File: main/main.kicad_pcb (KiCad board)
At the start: 2 copper layers, 1 part, among them M1 IDP_PROTOBOARD

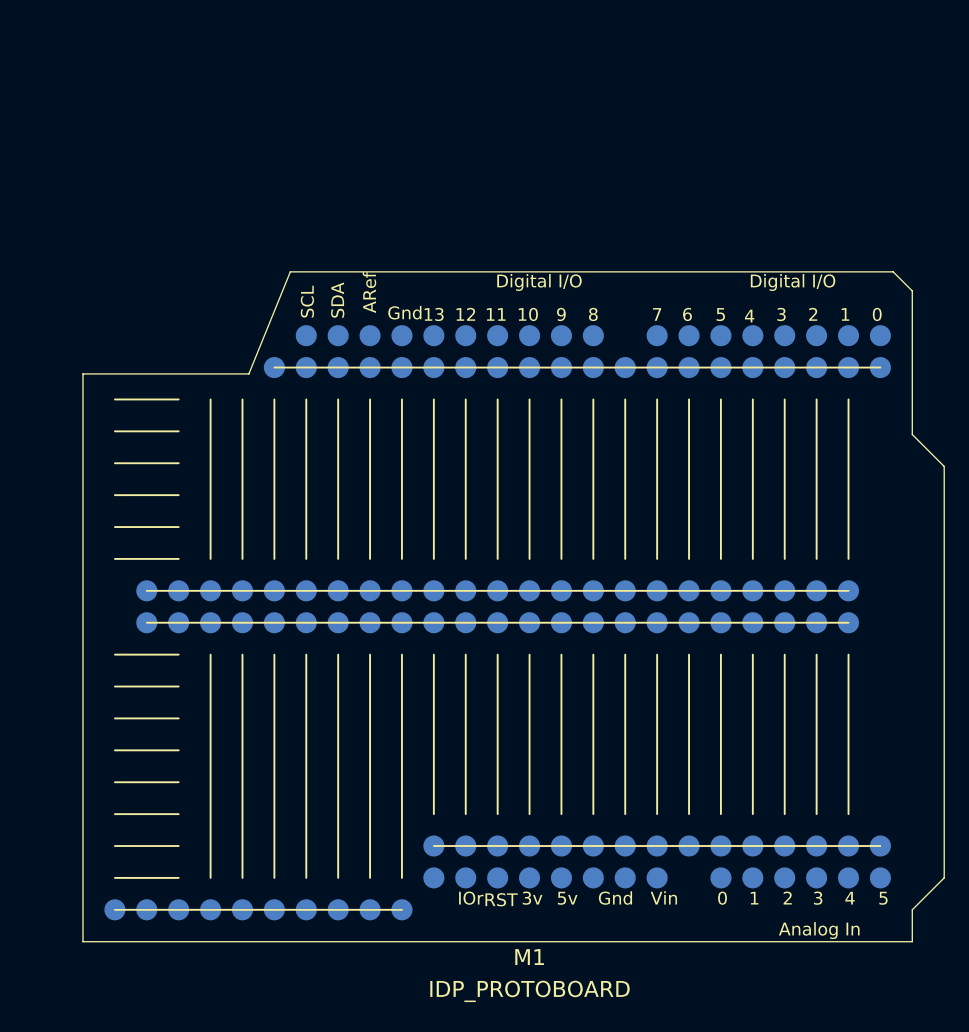
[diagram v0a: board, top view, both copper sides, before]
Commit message: First draft of Main PCB and Color Sensors PCB
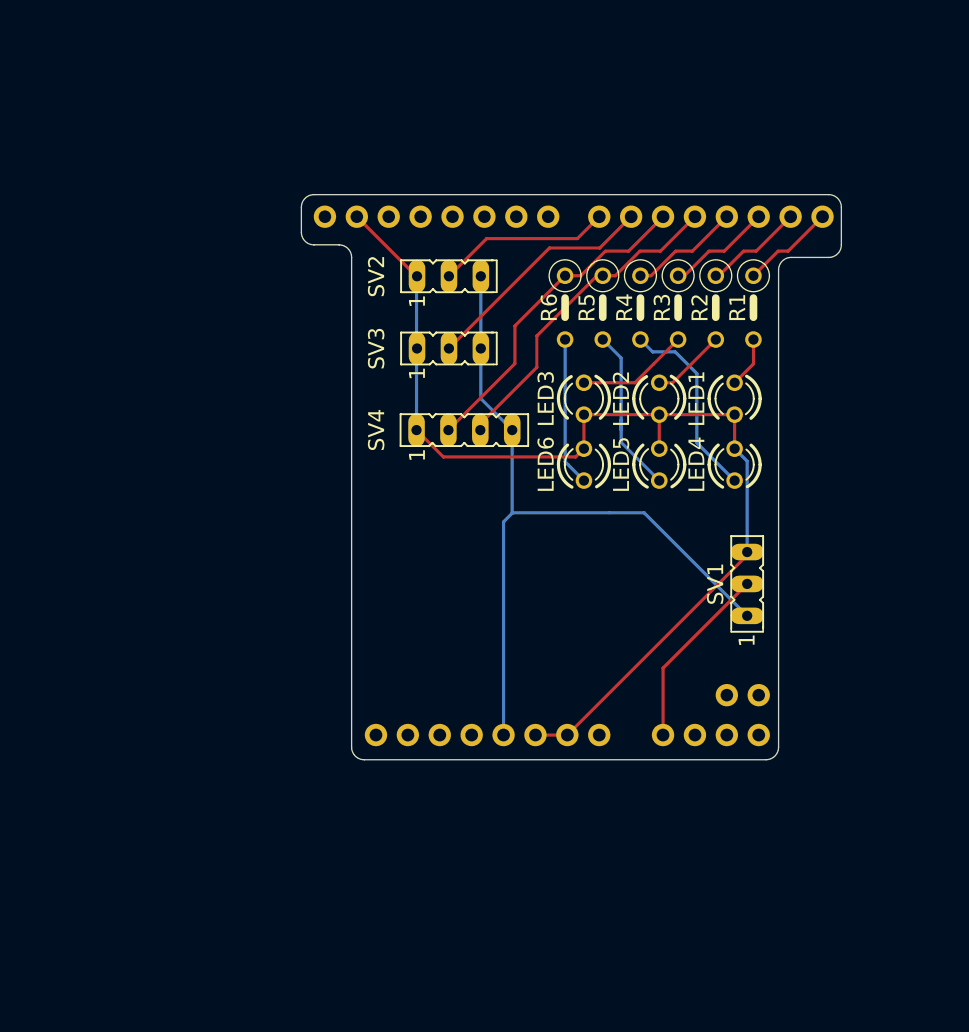
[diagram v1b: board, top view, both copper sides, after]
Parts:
- removed M1: IDP_PROTOBOARD, IDP_library_IDP_PROTO
- added CN1: 1X4-CLEANBIG, Adafruit Motor Shield v2.3:1X04-CLEANBIG, F.Cu at (104.6, 94.0)
- added D0-1: PINHD-1X8CLEANBIG, Adafruit Motor Shield v2.3:1X08-CLEANBIG, F.Cu at (104.6, 52.8)
- added JP2: HEADER-1X2ROUND, Adafruit Motor Shield v2.3:1X02_ROUND, F.Cu at (107.2, 90.9)
- added JP3: PINHD-1X8CLEANBIG, Adafruit Motor Shield v2.3:1X08-CLEANBIG, F.Cu at (86.8, 94.0)
- added JP4: HEADER-1X1070MIL, Adafruit Motor Shield v2.3:1X10_ROUND70, F.Cu at (80.2, 52.8)
- added LED1: LED_23MM, IDP:IDP_library_LED3MM, F.Cu at (106.5, 67.2)
- added LED2: LED_23MM, IDP:IDP_library_LED3MM, F.Cu at (100.5, 67.2)
- added LED3: LED_23MM, IDP:IDP_library_LED3MM, F.Cu at (94.5, 67.2)
- added LED4: LED_23MM, IDP:IDP_library_LED3MM, F.Cu at (106.5, 72.5)
- added LED5: LED_23MM, IDP:IDP_library_LED3MM, F.Cu at (100.5, 72.5)
- added LED6: LED_23MM, IDP:IDP_library_LED3MM, F.Cu at (94.5, 72.5)
- added R1: R-EU_0207_5V, IDP:IDP_library_0207_5V, F.Cu at (108.0, 60.0)
- added R2: R-EU_0207_5V, IDP:IDP_library_0207_5V, F.Cu at (105.0, 60.0)
- added R3: R-EU_0207_5V, IDP:IDP_library_0207_5V, F.Cu at (102.0, 60.0)
- added R4: R-EU_0207_5V, IDP:IDP_library_0207_5V, F.Cu at (99.0, 60.0)
- added R5: R-EU_0207_5V, IDP:IDP_library_0207_5V, F.Cu at (96.0, 60.0)
- added R6: R-EU_0207_5V, IDP:IDP_library_0207_5V, F.Cu at (93.0, 60.0)
- added SV1: FE03-1, IDP:IDP_library_FE03-1, F.Cu at (107.5, 82.0)
- added SV2: FE03-1, IDP:IDP_library_FE03-1, F.Cu at (83.8, 57.5)
- added SV3: FE03-1, IDP:IDP_library_FE03-1, F.Cu at (83.8, 63.2)
- added SV4: FE04-1, IDP:IDP_library_FE04-1, F.Cu at (86.2, 69.8)
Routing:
- net GND: track 0.00 -> 85.9 mm
- net +5V: track 0.00 -> 60.0 mm
- net /red: track 0.00 -> 25.9 mm
- net /green: track 0.00 -> 25.9 mm
- net /ultrasonic_right: track 0.00 -> 18.9 mm
- net Net-(LED4-PadA): track 0.00 -> 15.4 mm
- net /infra_red: track 0.00 -> 14.8 mm
- net /ultrasonic_left: track 0.00 -> 13.9 mm
- net Net-(LED5-PadA): track 0.00 -> 13.9 mm
- net Net-(LED6-PadA): track 0.00 -> 11.9 mm
- net Net-(LED3-PadA): track 0.00 -> 8.92 mm
- net /proximity: track 0.00 -> 8.83 mm
- net /status_2: track 0.00 -> 7.87 mm
- net /status_1: track 0.00 -> 7.66 mm
- net /status_0: track 0.00 -> 7.45 mm
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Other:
- board outline added: 43 x 45 mm
- copper layers 2 -> 16

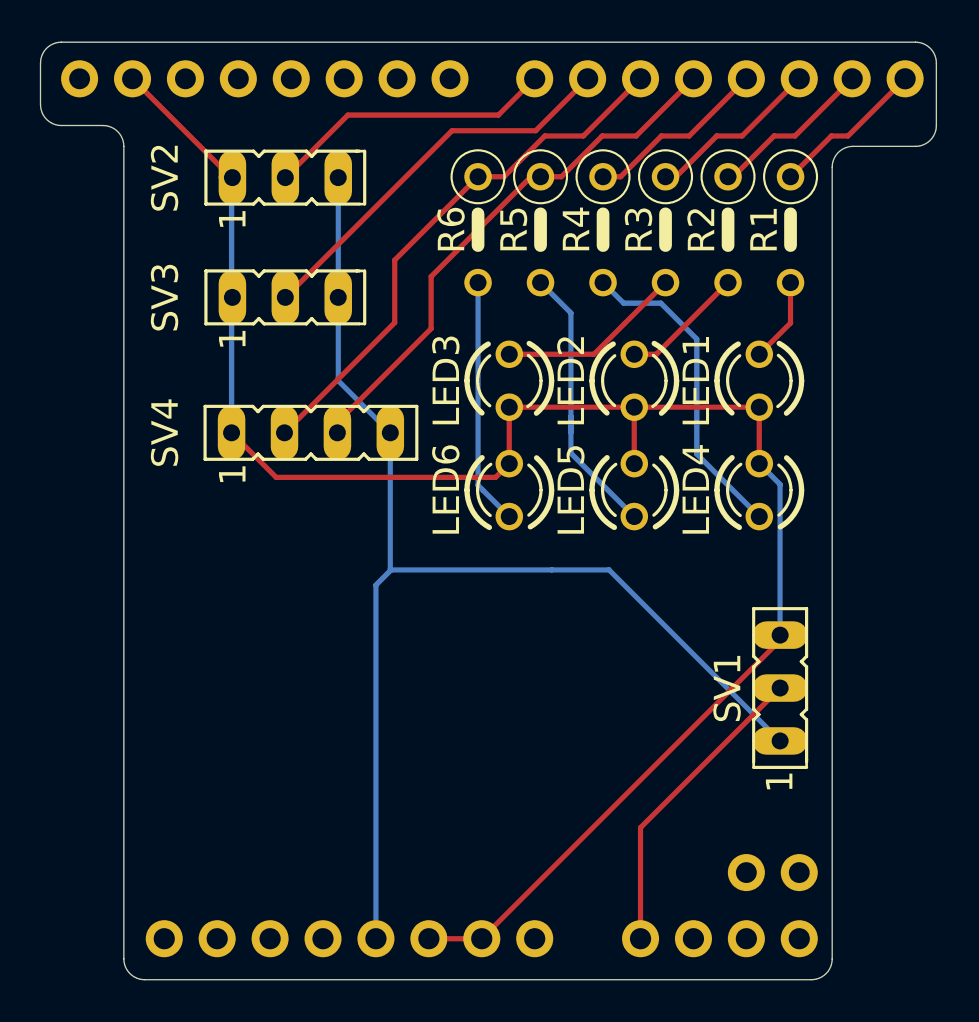
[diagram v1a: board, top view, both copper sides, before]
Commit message: Specify resistors; neaten silkscreen; improve 3D model
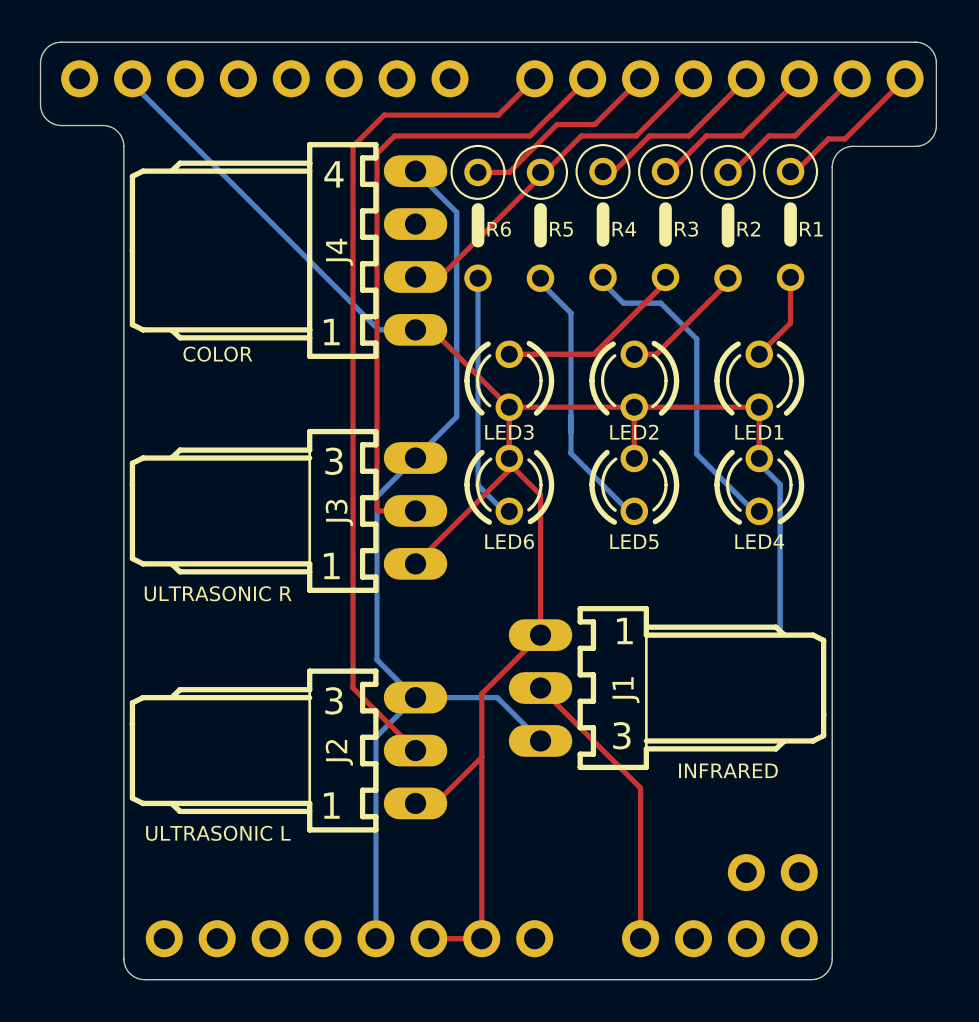
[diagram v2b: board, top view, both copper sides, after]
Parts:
- removed SV1, SV2, SV3: FE03-1, IDP:IDP_library_FE03-1
- removed SV4: FE04-1, IDP:IDP_library_FE04-1
- added J1: 22-05-7038-03, IDP:IDP_library_7395-03, F.Cu at (96.0, 82.0)
- added J2: 22-05-7038-03, IDP:IDP_library_7395-03, F.Cu at (90.0, 85.0)
- added J3: 22-05-7038-03, IDP:IDP_library_7395-03, F.Cu at (90.0, 73.5)
- added J4: 22-05-7048-04, IDP:IDP_library_7395-04, F.Cu at (90.0, 61.0)
- LED1, LED2, LED3: value LED_23MM -> BLUE_3MM
- LED4: value LED_23MM -> YELLOW_3MM
- LED5: value LED_23MM -> RED_3MM
- LED6: value LED_23MM -> GREEN_3MM
- R1, R2, R3, R4, R5, R6: value R-EU_0207_5V -> 270R
- moved LED4 0.25 mm to (106.5, 72.2)
- moved LED5 0.25 mm to (100.5, 72.2)
- moved LED6 0.25 mm to (94.5, 72.2)
- moved R1 0.25 mm to (108.0, 59.8)
- moved R3 0.25 mm to (102.0, 59.8)
- moved R4 0.25 mm to (99.0, 59.8)
- moved R2 0.21 mm to (105.0, 59.8)
- moved R5 0.21 mm to (96.0, 59.8)
- moved R6 0.21 mm to (93.0, 59.8)
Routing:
- net /ultrasonic_left: track 13.9 -> 40.3 mm
- net /green: track 25.9 -> 9.66 mm
- net +5V: track 60.0 -> 47.7 mm
- net /ultrasonic_right: track 18.9 -> 30.6 mm
- net /red: track 25.9 -> 17.3 mm
- net GND: track 85.9 -> 91.4 mm
- net /infra_red: track 14.8 -> 14.0 mm
- net /status_2: track 7.87 -> 8.37 mm
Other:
- board text added: "COLOR"
- board text added: "INFRARED"
- board text added: "ULTRASONIC L"
- board text added: "ULTRASONIC R"

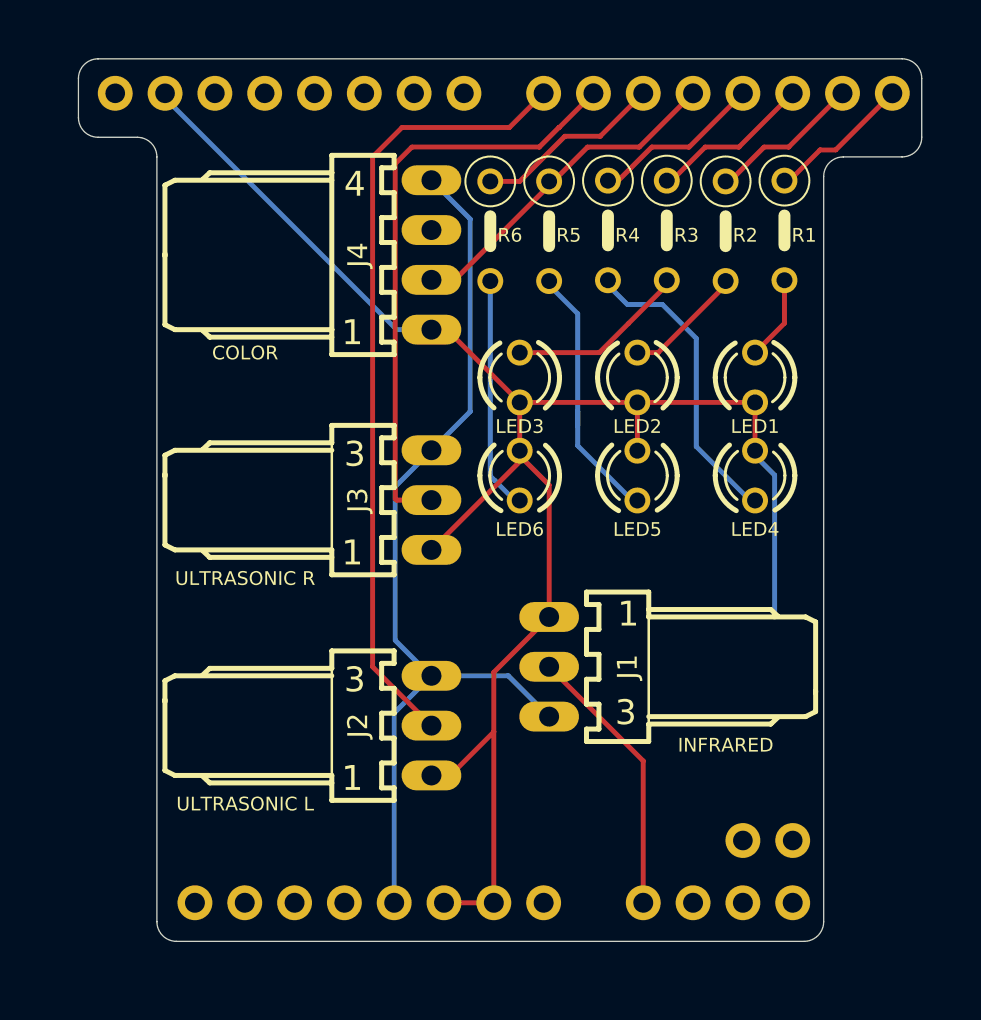
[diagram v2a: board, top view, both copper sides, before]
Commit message: Add power and ground planes; update resistor values
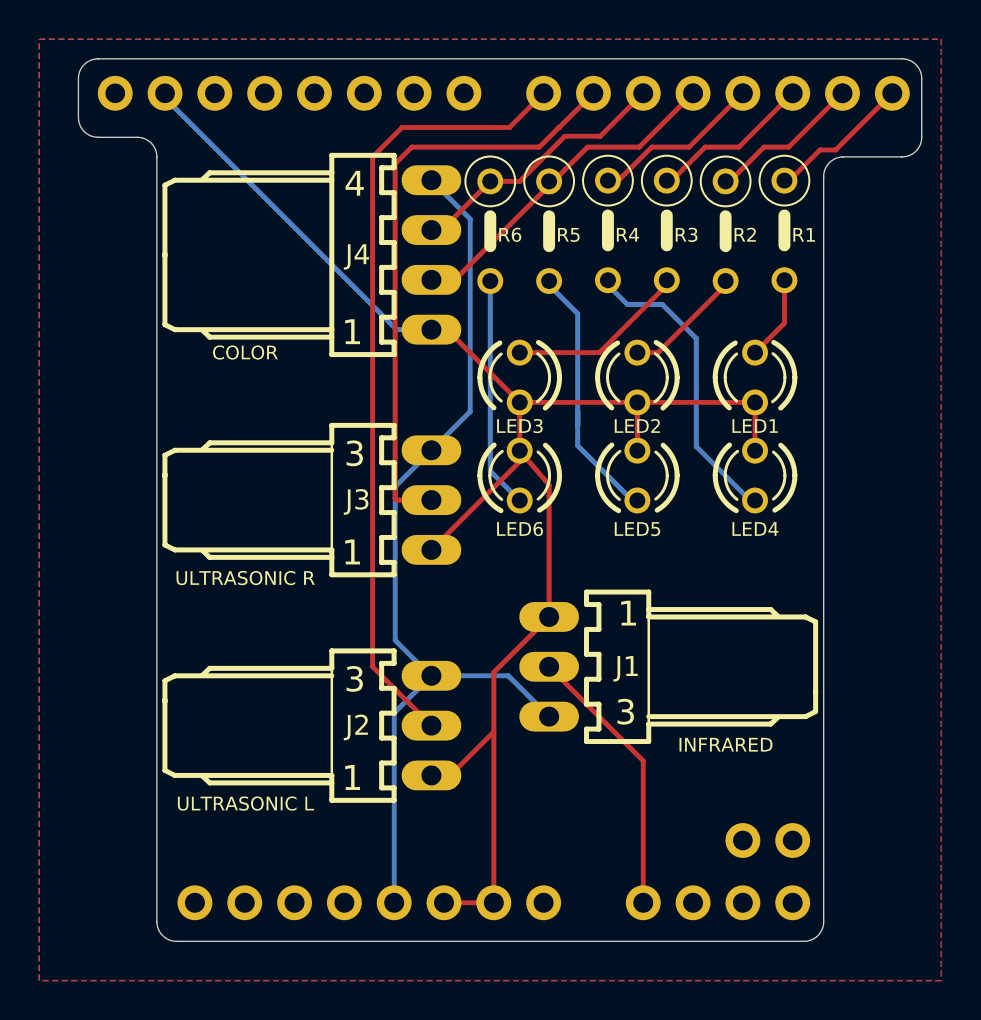
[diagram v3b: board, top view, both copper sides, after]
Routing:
- net GND: track 91.4 -> 83.0 mm
- net /green: track 9.66 -> 13.7 mm
- added copper zone on B.Cu, net +5V
- added copper zone on F.Cu, net GND

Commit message: Submission candidate 1
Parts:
- moved R1 20.2 mm to (88.0, 62.3)
- moved R3 20.2 mm to (82.0, 62.3)
- moved R4 20.2 mm to (79.0, 62.3)
- moved CN1 20.2 mm to (84.6, 96.5)
- moved D0-1 20.2 mm to (84.6, 55.3)
- moved J1 20.2 mm to (76.0, 84.5)
- moved J2 20.2 mm to (70.0, 87.5)
- moved J3 20.2 mm to (70.0, 76.0)
- moved J4 20.2 mm to (70.0, 63.5)
- moved JP2 20.2 mm to (87.2, 93.4)
- moved JP3 20.2 mm to (66.8, 96.5)
- moved JP4 20.2 mm to (60.2, 55.3)
- moved LED1 20.2 mm to (86.5, 69.8)
- moved LED2 20.2 mm to (80.5, 69.8)
- moved LED3 20.2 mm to (74.5, 69.8)
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
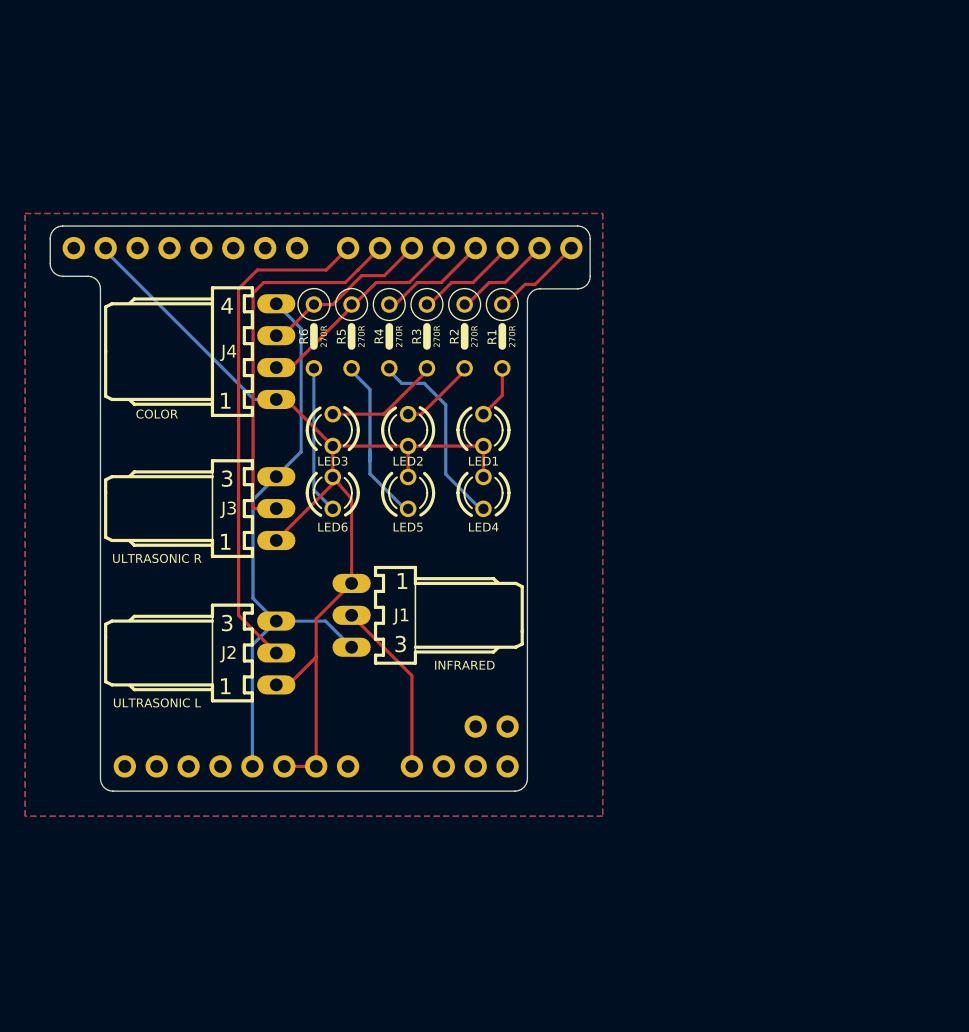
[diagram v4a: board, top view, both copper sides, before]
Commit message: Add PDF versions of schematics
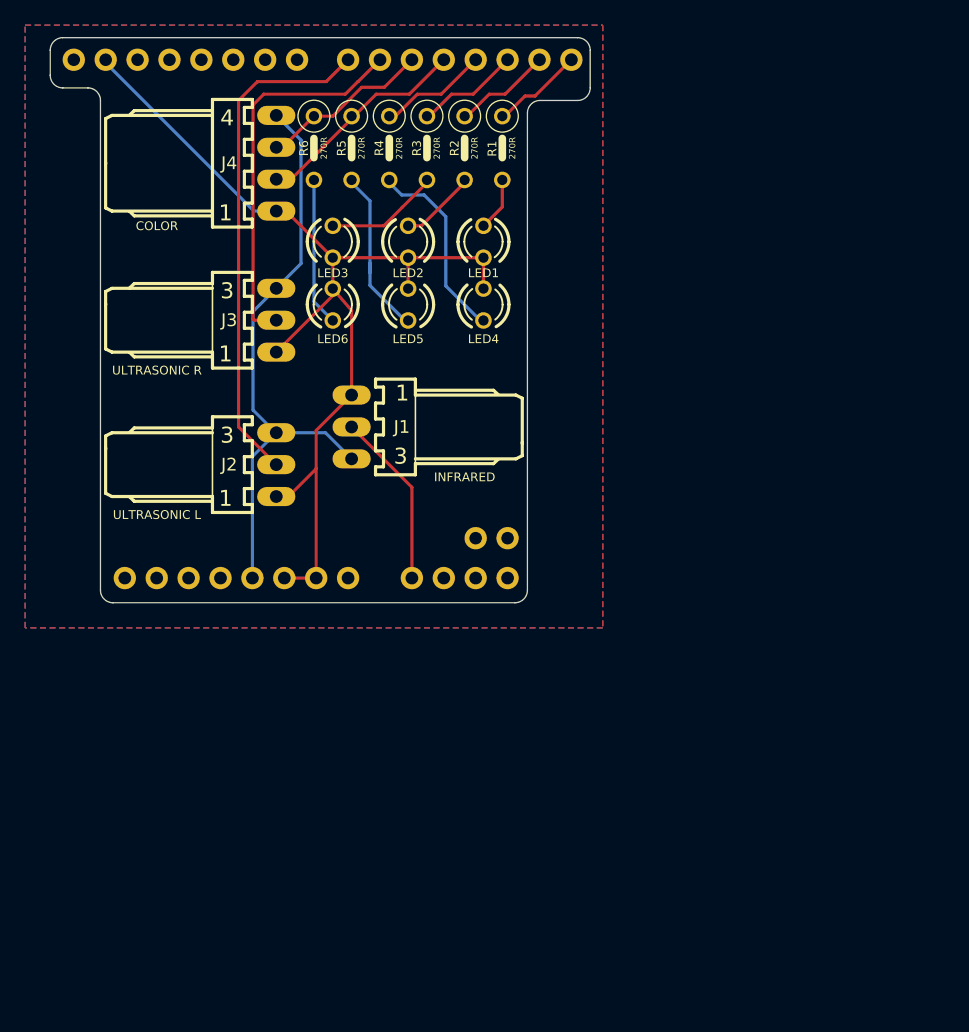
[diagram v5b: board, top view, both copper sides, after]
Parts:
- moved CN1 15.0 mm to (84.6, 81.5)
- moved D0-1 15.0 mm to (84.6, 40.3)
- moved J1 15.0 mm to (76.0, 69.5)
- moved J2 15.0 mm to (70.0, 72.5)
- moved J3 15.0 mm to (70.0, 61.0)
- moved J4 15.0 mm to (70.0, 48.5)
- moved JP2 15.0 mm to (87.2, 78.4)
- moved JP3 15.0 mm to (66.8, 81.5)
- moved JP4 15.0 mm to (60.2, 40.3)
- moved LED1 15.0 mm to (86.5, 54.8)
- moved LED2 15.0 mm to (80.5, 54.8)
- moved LED3 15.0 mm to (74.5, 54.8)
- moved LED4 15.0 mm to (86.5, 59.8)
- moved LED5 15.0 mm to (80.5, 59.8)
- moved LED6 15.0 mm to (74.5, 59.8)
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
